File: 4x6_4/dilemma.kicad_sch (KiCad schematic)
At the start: 361 parts, among them J1 USB_C_Receptacle_USB2.0, J102 NA_serial, J105 NA_Conn_01x04_Female, J113 Cirque, J3 NA_GC9A01, J4 Conn_01x05, J5 NA_Conn_01x02, J5001 USB_C_Receptacle_USB2.0, J5002 NA_Conn_01x02, J5003 NA_serial, J5004 NA_GC9A01, J5005 NA_Conn_01x04_Female, J5006 Conn_01x01_Socket, J5007 Cirque, J5008 Conn_01x05, J5009 Conn_01x05, J5010 Conn_01x05, J5011 Conn_01x01_Socket, J5012 Conn_01x01_Socket, J5013 Conn_01x01_Socket, J5014 Conn_01x01_Socket, J5015 Conn_01x01_Socket, J5016 Conn_01x01_Socket, J5017 Conn_01x01_Socket, J5018 Conn_01x01_Socket, J5019 Conn_01x01_Socket, J5020 Conn_01x01_Socket, J5021 Conn_01x01_Socket, SW1 SW_Push, SW101 NA_SW_Push, SW102 NA_SW_Push, SW103 NA_SW_Push, SW104 NA_SW_Push, SW105 NA_SW_Push, SW106 NA_SW_Push, SW107 NA_SW_Push, SW108 NA_SW_Push, SW109 NA_SW_Push, SW112 NA_SW_Push, SW113 NA_SW_Push, SW114 NA_SW_Push, SW115 NA_SW_Push, SW116 NA_SW_Push, SW117 NA_SW_Push, SW118 NA_SW_Push, SW119 NA_SW_Push, SW3001 NA_SW_Push, SW3002 NA_RotaryEncoder_Switch, SW5001 SW_Push, SW5002 NA_SW_Push, SW5003 NA_SW_Push, SW5004 NA_SW_Push, SW5005 NA_SW_Push, SW5006 NA_SW_Push, SW5007 NA_SW_Push, SW5008 NA_SW_Push, SW5009 NA_SW_Push, SW5010 NA_SW_Push, SW5011 NA_SW_Push, SW5012 NA_SW_Push, SW5013 NA_SW_Push, SW5014 NA_SW_Push, SW5015 NA_SW_Push, SW5016 NA_SW_Push, SW5017 NA_SW_Push, SW5018 NA_SW_Push, SW5019 NA_SW_Push, SW5020 NA_RotaryEncoder_Switch, SW5021 SW_SPST, SW5022 SW_SPST, SW5023 NA_SW_Push, SW5024 NA_SW_Push, SW5025 NA_SW_Push, SW5026 NA_SW_Push, SW5027 NA_SW_Push, SW5028 NA_SW_Push, SW5029 NA_SW_Push, SW5030 NA_SW_Push, SW5031 NA_SW_Push, SW5032 NA_SW_Push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

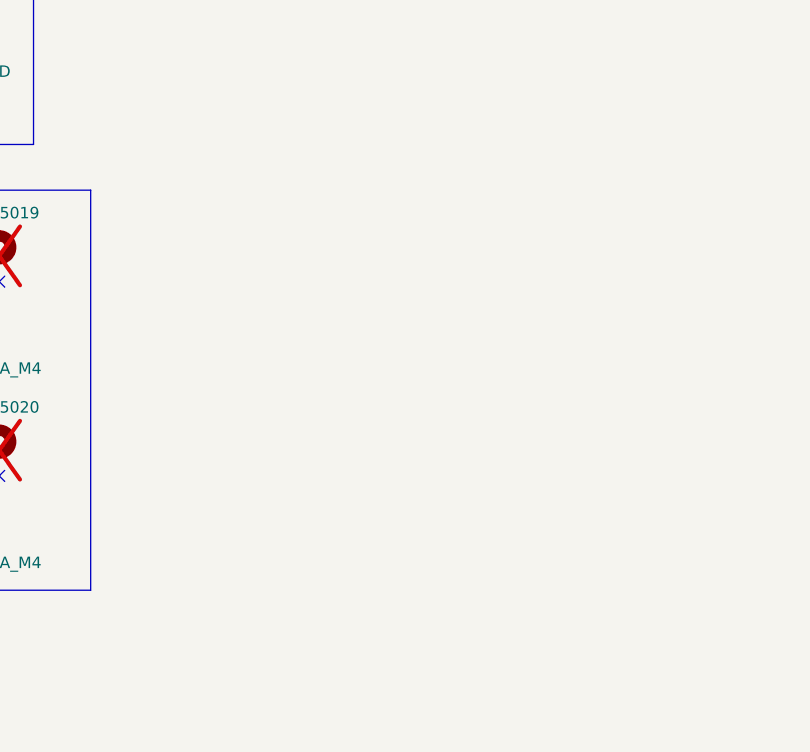
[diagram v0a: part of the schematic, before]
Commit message: mousebites around PCB
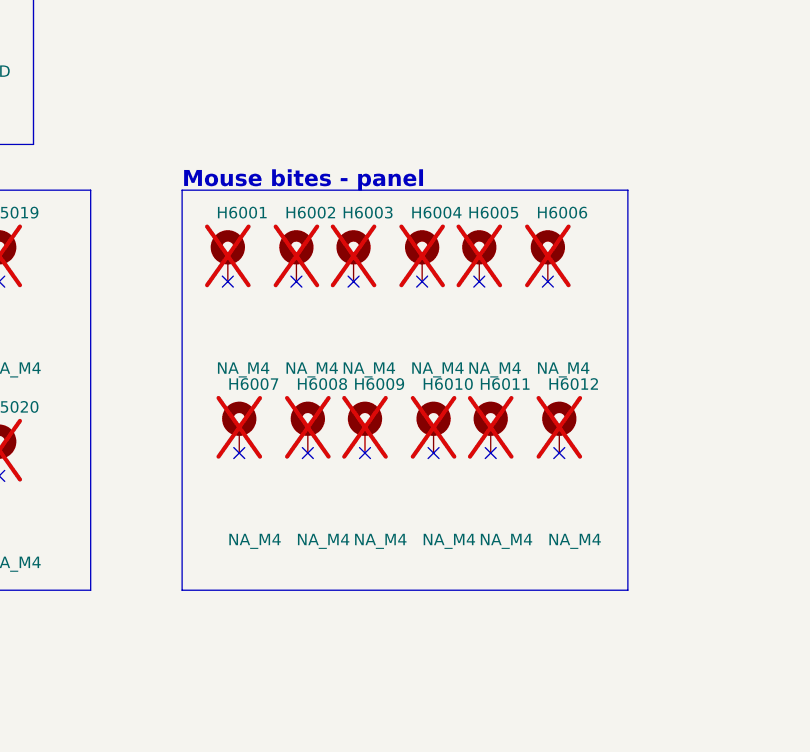
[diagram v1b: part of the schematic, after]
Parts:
- added H6001, H6002, H6003, H6004, H6005, H6006, H6007, H6008, H6009, H6010, H6011, H6012: NA_M4, local-libraries:mousebite, symbol Mechanical:MountingHole_Pad
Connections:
- no-connect marks 35 -> 47
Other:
- note added: "Mouse bites - panel"
